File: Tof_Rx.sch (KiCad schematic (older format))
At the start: 105 parts, among them M3 mounting_holes_laser, M4 mounting_holes_laser, U15 LMH6559MF, U16 SiPM-MicroRB, U17 UMCC_50Ohm, U18 ts5a4596, U19 ts5a4596, U20 MAX40659, U21 LP5907MFX-3.3_NOPB, U22 UMCC_50Ohm, U23 TLV3501, U24 TLV3501, U25 HMC589AST89E, U26 NC7WZ00K8X, U27 UMCC_50Ohm, U28 UMCC_50Ohm, U29 UMCC_50Ohm, U30 NC7WZ00K8X, U32 UMCC_50Ohm, U35 UMCC_50Ohm

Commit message: Version 1.0. As ordered at PCBWay on 13.11.2019
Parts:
- renumbered C27 to C46, C28 to C47, C68 to C48, C69 to C49, C29 to C50, C71 to C51, C30 to C52, C72 to C53, C31 to C54, C32 to C55, C33 to C56, C34 to C57, C35 to C58, C36 to C59, C37 to C60, C38 to C61, C39 to C62, C40 to C63, C41 to C64, C44 to C65, C46 to C66, C62 to C67, C63 to C68, C45 to C69, C49 to C70, C70 to C71, C48 to C72, C47 to C73, C51 to C74, C50 to C75, C54 to C76, C52 to C77, C57 to C78, C53 to C79, C64 to C80, C77 to C81, C58 to C82, C81 to C83, D3 to D5, D4 to D6, L12 to L13, L13 to L14, L16 to L15, L14 to L16, L15 to L19, L19 to L20, L20 to L21, L21 to L22, R50 to R63, R51 to R64, R14 to R65, R52 to R66, R54 to R67, R53 to R68, R56 to R69, R55 to R70, R57 to R71, R58 to R72, R59 to R73, R60 to R74, R63 to R75, R61 to R76, R64 to R77, R62 to R78, R67 to R79, R76 to R80, R77 to R81, R88 to R82, R66 to R83, R68 to R84, R69 to R85, R78 to R86, R89 to R87, R90 to R88, R91 to R89, R79 to R90, R72 to R91, R70 to R92, TP4 to TP10, TP5 to TP11, TP6 to TP12, TP10 to TP13, TP9 to TP14, U32 to U18, U15 to U19, U16 to U20, U17 to U21, U18 to U22, U19 to U23, U21 to U24, U20 to U25, U22 to U26, U30 to U27, U26 to U27, U23 to U28, U24 to U29, U25 to U30, U26 to U31, U30 to U31, U35 to U32, U27 to U33, U28 to U34, U29 to U35

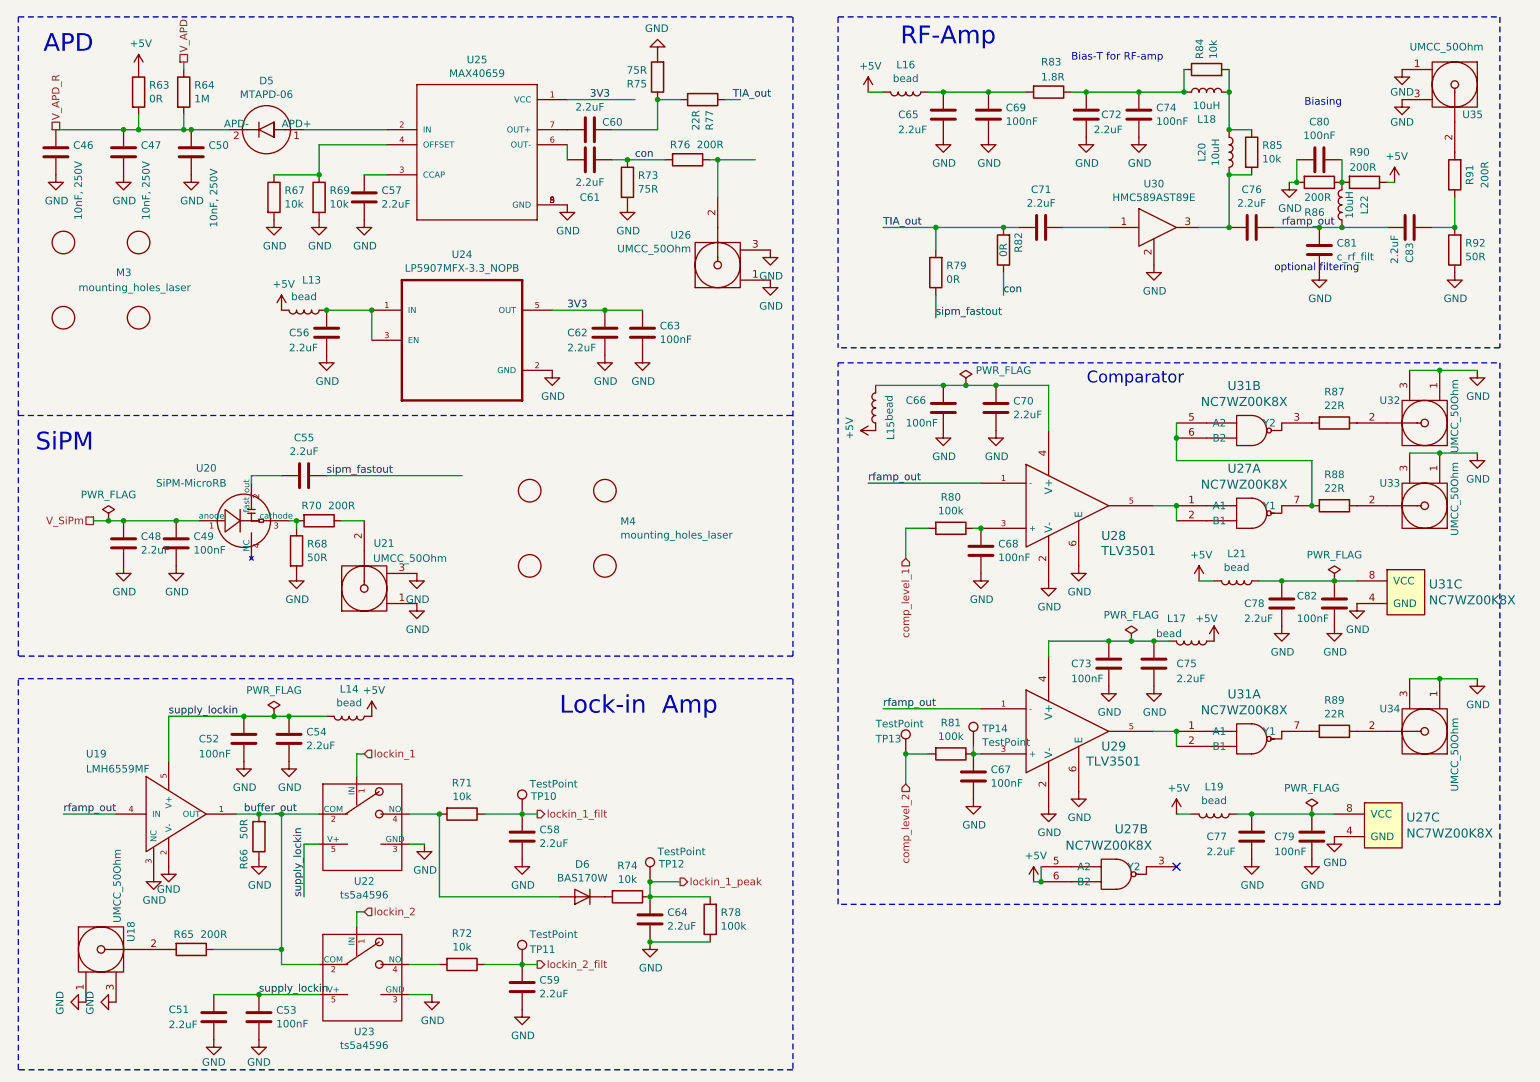
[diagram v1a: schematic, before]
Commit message: This is the actual pcb ordered by PCBWay 13.11.2019 The last commit had an error in the schematic files
Revert "Version 1.0. As ordered at PCBWay on 13.11.2019"

This reverts commit d90296e8e464a35f67a5ff7ebe731cf47d5f6555.
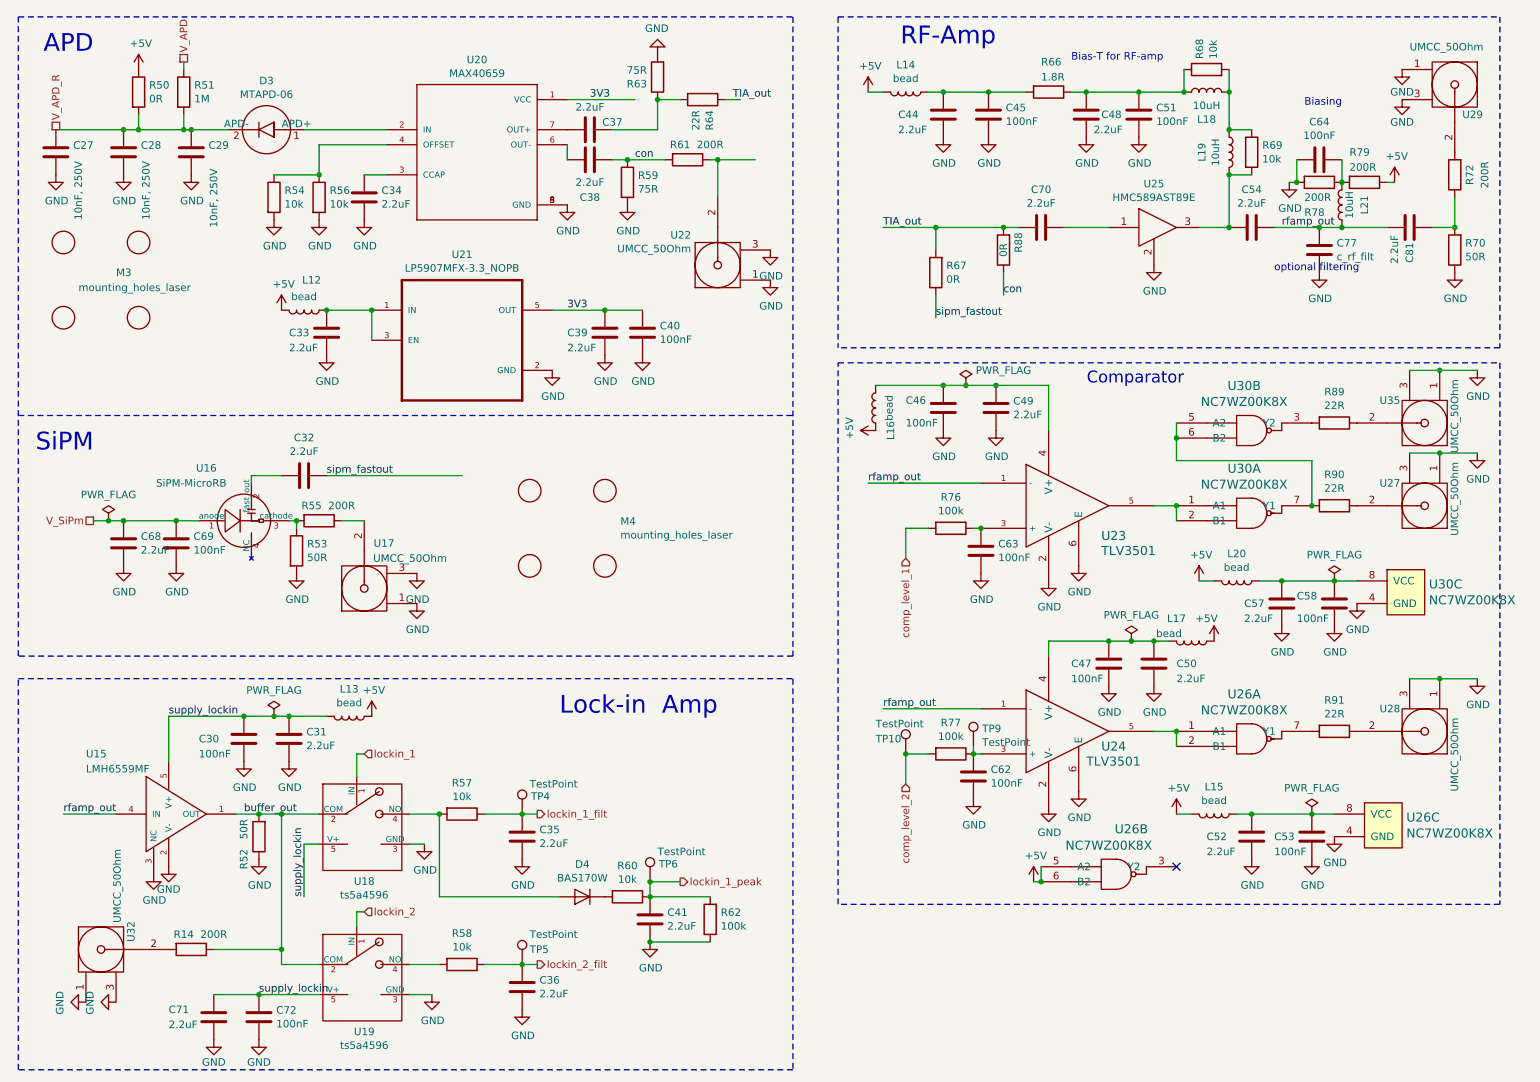
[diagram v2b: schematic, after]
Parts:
- renumbered C46 to C27, C47 to C28, C50 to C29, C52 to C30, C54 to C31, C55 to C32, C56 to C33, C57 to C34, C58 to C35, C59 to C36, C60 to C37, C61 to C38, C62 to C39, C63 to C40, C64 to C41, C65 to C44, C69 to C45, C66 to C46, C73 to C47, C72 to C48, C70 to C49, C75 to C50, C74 to C51, C77 to C52, C79 to C53, C76 to C54, C78 to C57, C82 to C58, C67 to C62, C68 to C63, C80 to C64, C48 to C68, C49 to C69, C71 to C70, C51 to C71, C53 to C72, C81 to C77, C83 to C81, D5 to D3, D6 to D4, L13 to L12, L14 to L13, L16 to L14, L19 to L15, L15 to L16, L20 to L19, L21 to L20, L22 to L21, R65 to R14, R63 to R50, R64 to R51, R66 to R52, R68 to R53, R67 to R54, R70 to R55, R69 to R56, R71 to R57, R72 to R58, R73 to R59, R74 to R60, R76 to R61, R78 to R62, R75 to R63, R77 to R64, R83 to R66, R79 to R67, R84 to R68, R85 to R69, R92 to R70, R91 to R72, R80 to R76, R81 to R77, R86 to R78, R90 to R79, R82 to R88, R87 to R89, R88 to R90, R89 to R91, TP13 to TP10, TP10 to TP4, TP11 to TP5, TP12 to TP6, TP14 to TP9, U19 to U15, U20 to U16, U21 to U17, U22 to U18, U23 to U19, U25 to U20, U24 to U21, U26 to U22, U28 to U23, U29 to U24, U30 to U25, U31 to U26, U27 to U26, U33 to U27, U34 to U28, U35 to U29, U27 to U30, U31 to U30, U18 to U32, U32 to U35
